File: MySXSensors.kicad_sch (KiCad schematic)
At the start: 10 parts, among them J1 LD2410B, J2 UART, U1 BME280, U2 BH1750FVI-TR

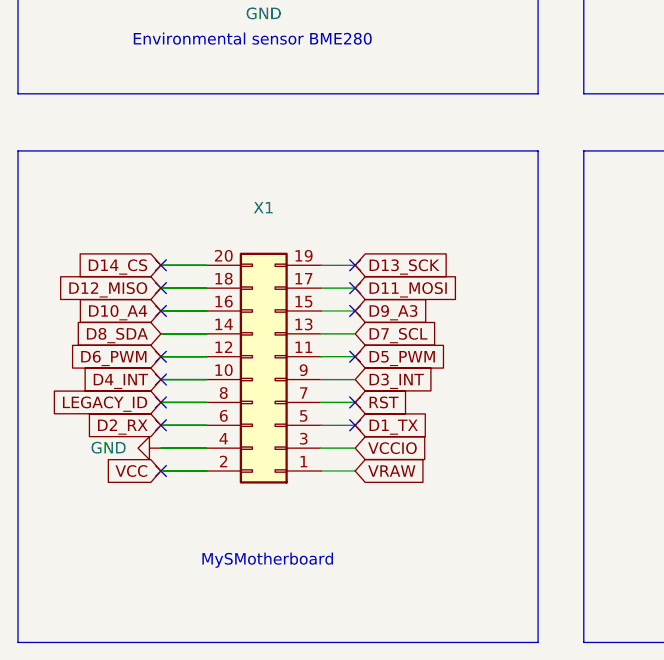
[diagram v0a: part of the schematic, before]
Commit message: add external connector for I2C
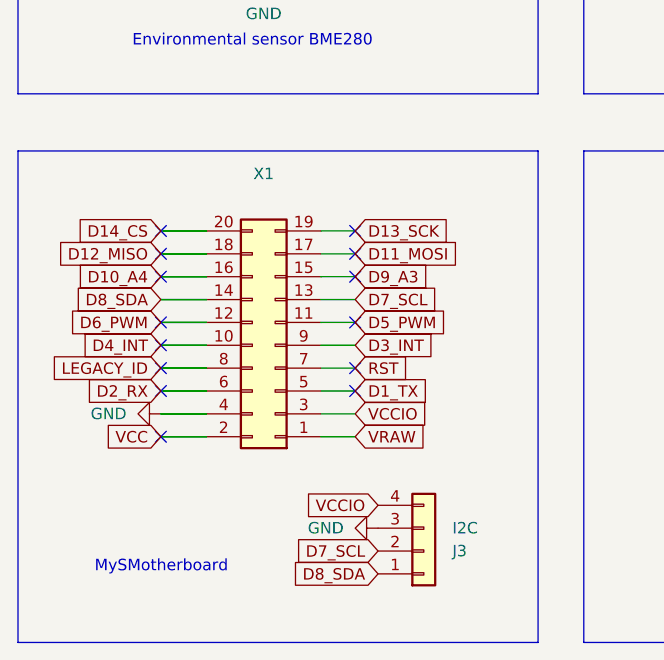
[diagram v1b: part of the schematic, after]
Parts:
- added J3: I2C, Connector_PinHeader_2.54mm:PinHeader_1x04_P2.54mm_Horizontal, symbol Connector_Generic:Conn_01x04
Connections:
- net D7_SCL: now also J3.2 (Pin_2)
- net D8_SDA: now also J3.1 (Pin_1)
- net GND: now also J3.3 (Pin_3)
- net VCCIO: now also J3.4 (Pin_4)
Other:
- moved on the sheet: X1

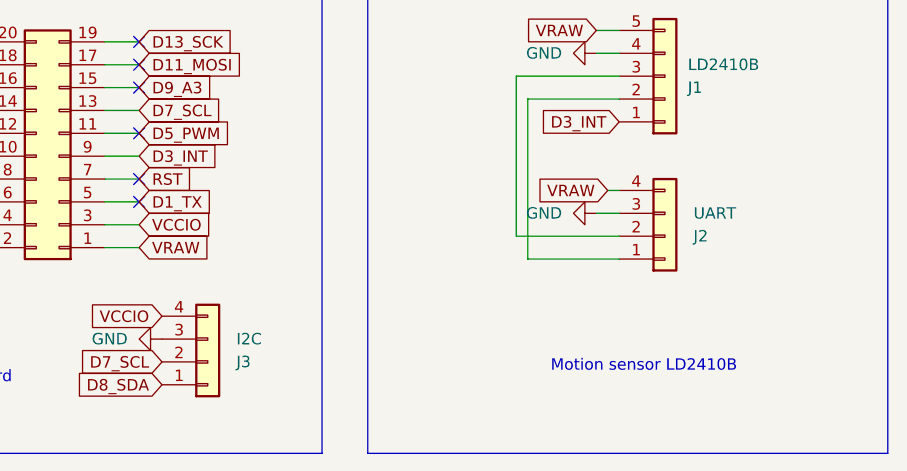
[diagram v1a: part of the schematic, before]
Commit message: add JST connector + pin headers for stability
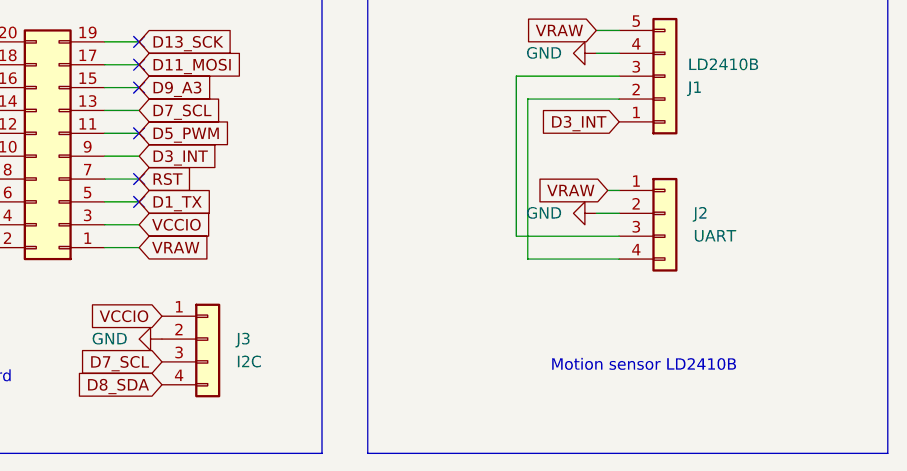
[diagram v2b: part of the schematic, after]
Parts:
- J2, J3: footprint Connector_PinHeader_2.54mm:PinHeader_1x04_P2.54mm_Horizontal -> MySXSensors:JST-XH_S_4P-2.54MM-PIN1-RIGHT
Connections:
- net D7_SCL: now also J3.3 (Pin_3); no longer J3.2 (Pin_2)
- net D8_SDA: now also J3.4 (Pin_4); no longer J3.1 (Pin_1)
- net GND: now also J2.2 (Pin_2), J3.2 (Pin_2); no longer J2.3 (Pin_3), J3.3 (Pin_3)
- net VCCIO: now also J3.1 (Pin_1); no longer J3.4 (Pin_4)
- net VRAW: now also J2.1 (Pin_1); no longer J2.4 (Pin_4)
- net at J1.2 (Pin_2): now also J2.4 (Pin_4); no longer J2.1 (Pin_1)
- net at J1.3 (Pin_3): now also J2.3 (Pin_3); no longer J2.2 (Pin_2)
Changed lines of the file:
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@@
 	(wire
 		(pts
-			(xy 151.13 130.81) (xy 162.56 130.81)
+			(xy 152.4 133.35) (xy 162.56 133.35)
 		)
 		(stroke
@@
 	(wire
 		(pts
-			(xy 160.02 128.27) (xy 162.56 128.27)
-		)
-		(stroke
-			(width 0)
-			(type default)
-		)
-	)
-	(wire
-		(pts
 			(xy 87.63 119.38) (xy 92.71 119.38)
 		)
@@
 	(wire
 		(pts
+			(xy 151.13 130.81) (xy 162.56 130.81)
+		)
+		(stroke
+			(width 0)
+			(type default)
+		)
+	)
+	(wire
+		(pts
 			(xy 87.63 124.46) (xy 92.71 124.46)
 		)
@@
 	(wire
 		(pts
+			(xy 160.02 128.27) (xy 162.56 128.27)
+		)
+		(stroke
+			(width 0)
+			(type default)
+		)
+	)
+	(wire
+		(pts
 			(xy 92.71 129.54) (xy 87.63 129.54)
 		)
@@
 	(wire
 		(pts
-			(xy 152.4 133.35) (xy 162.56 133.35)
-		)
-		(stroke
-			(width 0)
-			(type default)
-		)
-	)
-	(wire
-		(pts
 			(xy 83.82 49.53) (xy 96.52 49.53)
 		)
@@
 		(pts
 			(xy 99.06 49.53) (xy 101.6 49.53)
-		)
-		(stroke
-			(width 0)
-			(type default)
-		)
-	)
-	(wire
-		(pts
-			(xy 161.29 125.73) (xy 162.56 125.73)
 		)
 		(stroke
@@
 		(pts
 			(xy 92.71 109.22) (xy 87.63 109.22)
+		)
+		(stroke
+			(width 0)
+			(type default)
+		)
+	)
+	(wire
+		(pts
+			(xy 162.56 125.73) (xy 161.29 125.73)
 		)
 		(stroke
@@
 	(symbol
 		(lib_id "Connector_Generic:Conn_01x04")
-		(at 167.64 130.81 0)
-		(mirror x)
+		(at 167.64 128.27 0)
 		(unit 1)
 		(exclude_from_sim no)
@@
 		(dnp no)
 		(property "Reference" "J2"
+			(at 170.815 128.27 0)
+			(effects
+				(font
+					(size 1.27 1.27)
+				)
+				(justify left)
+			)
+		)
+		(property "Value" "UART"
 			(at 170.815 130.81 0)
 			(effects
@@
 			)
 		)
-		(property "Value" "UART"
-			(at 170.815 128.27 0)
-			(effects
-				(font
-					(size 1.27 1.27)
-				)
-				(justify left)
-			)
-		)
-		(property "Footprint" "Connector_PinHeader_2.54mm:PinHeader_1x04_P2.54mm_Horizontal"
-			(at 167.64 130.81 0)
+		(property "Footprint" "MySXSensors:JST-XH_S_4P-2.54MM-PIN1-RIGHT"
+			(at 167.64 128.27 0)
 			(effects
 				(font
@@
 		)
 		(property "Datasheet" "~"
-			(at 167.64 130.81 0)
+			(at 167.64 128.27 0)
 			(effects
 				(font
@@
 		)
 		(property "Description" ""
-			(at 167.64 130.81 0)
+			(at 167.64 128.27 0)
 			(effects
 				(font
@@
 	(symbol
 		(lib_id "Connector_Generic:Conn_01x04")
-		(at 116.84 144.78 0)
-		(mirror x)
+		(at 116.84 142.24 0)
 		(unit 1)
 		(exclude_from_sim no)
@@
 		(dnp no)
 		(property "Reference" "J3"
+			(at 120.015 142.24 0)
+			(effects
+				(font
+					(size 1.27 1.27)
+				)
+				(justify left)
+			)
+		)
+		(property "Value" "I2C"
 			(at 120.015 144.78 0)
 			(effects
@@
 			)
 		)
-		(property "Value" "I2C"
-			(at 120.015 142.24 0)
-			(effects
-				(font
-					(size 1.27 1.27)
-				)
-				(justify left)
-			)
-		)
-		(property "Footprint" "Connector_PinHeader_2.54mm:PinHeader_1x04_P2.54mm_Horizontal"
-			(at 116.84 144.78 0)
+		(property "Footprint" "MySXSensors:JST-XH_S_4P-2.54MM-PIN1-RIGHT"
+			(at 116.84 142.24 0)
 			(effects
 				(font
@@
 		)
 		(property "Datasheet" "~"
-			(at 116.84 144.78 0)
+			(at 116.84 142.24 0)
 			(effects
 				(font
@@
 		)
 		(property "Description" ""
-			(at 116.84 144.78 0)
-			(effects
-				(font
+			(at 116.84 142.24 0)
+			(effects
+				(font

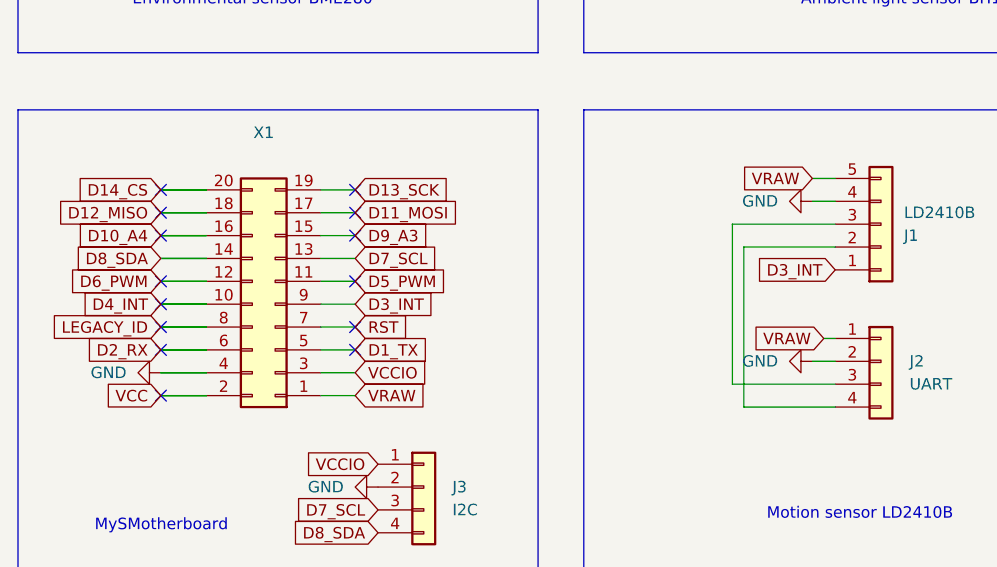
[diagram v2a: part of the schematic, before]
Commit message: change motion signal assignment to D4_INT
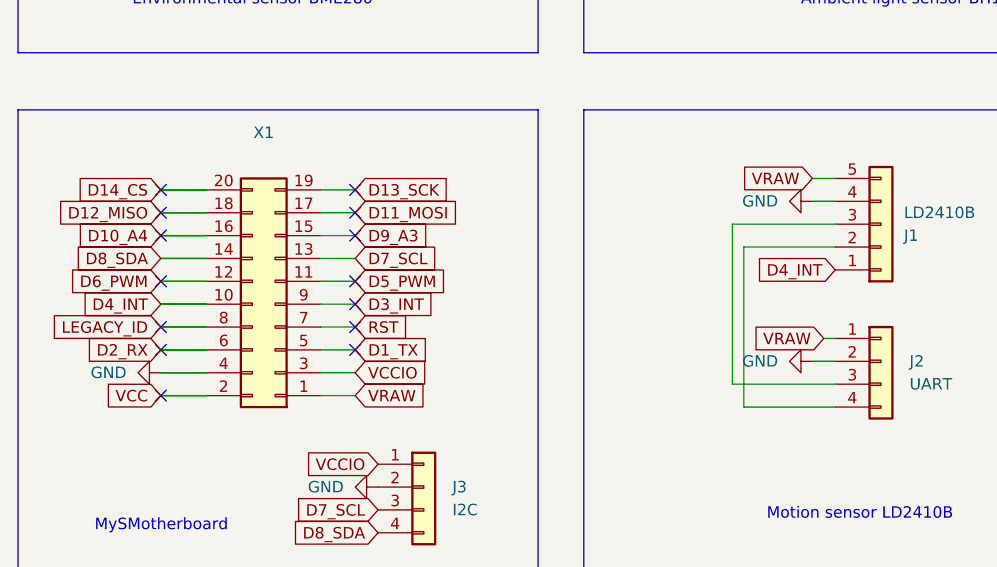
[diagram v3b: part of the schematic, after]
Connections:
- net D3_INT: no longer J1.1 (Pin_1)
- net D4_INT: now also J1.1 (Pin_1)
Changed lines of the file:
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@@
-	)
-	(no_connect
-		(at 87.63 121.92)
 	)
 	(no_connect
@@
 	(no_connect
 		(at 109.22 124.46)
+	)
+	(no_connect
+		(at 109.22 121.92)
 	)
 	(no_connect
@@
 		)
 	)
-	(global_label "D3_INT"
+	(global_label "D4_INT"
 		(shape input)
 		(at 162.56 118.11 180)
